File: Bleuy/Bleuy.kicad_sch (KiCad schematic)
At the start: 23 parts, among them J1 Conn_Coaxial, U1 STM32WB55CEU6, X1 32 MHz, X2 32.768 kHz

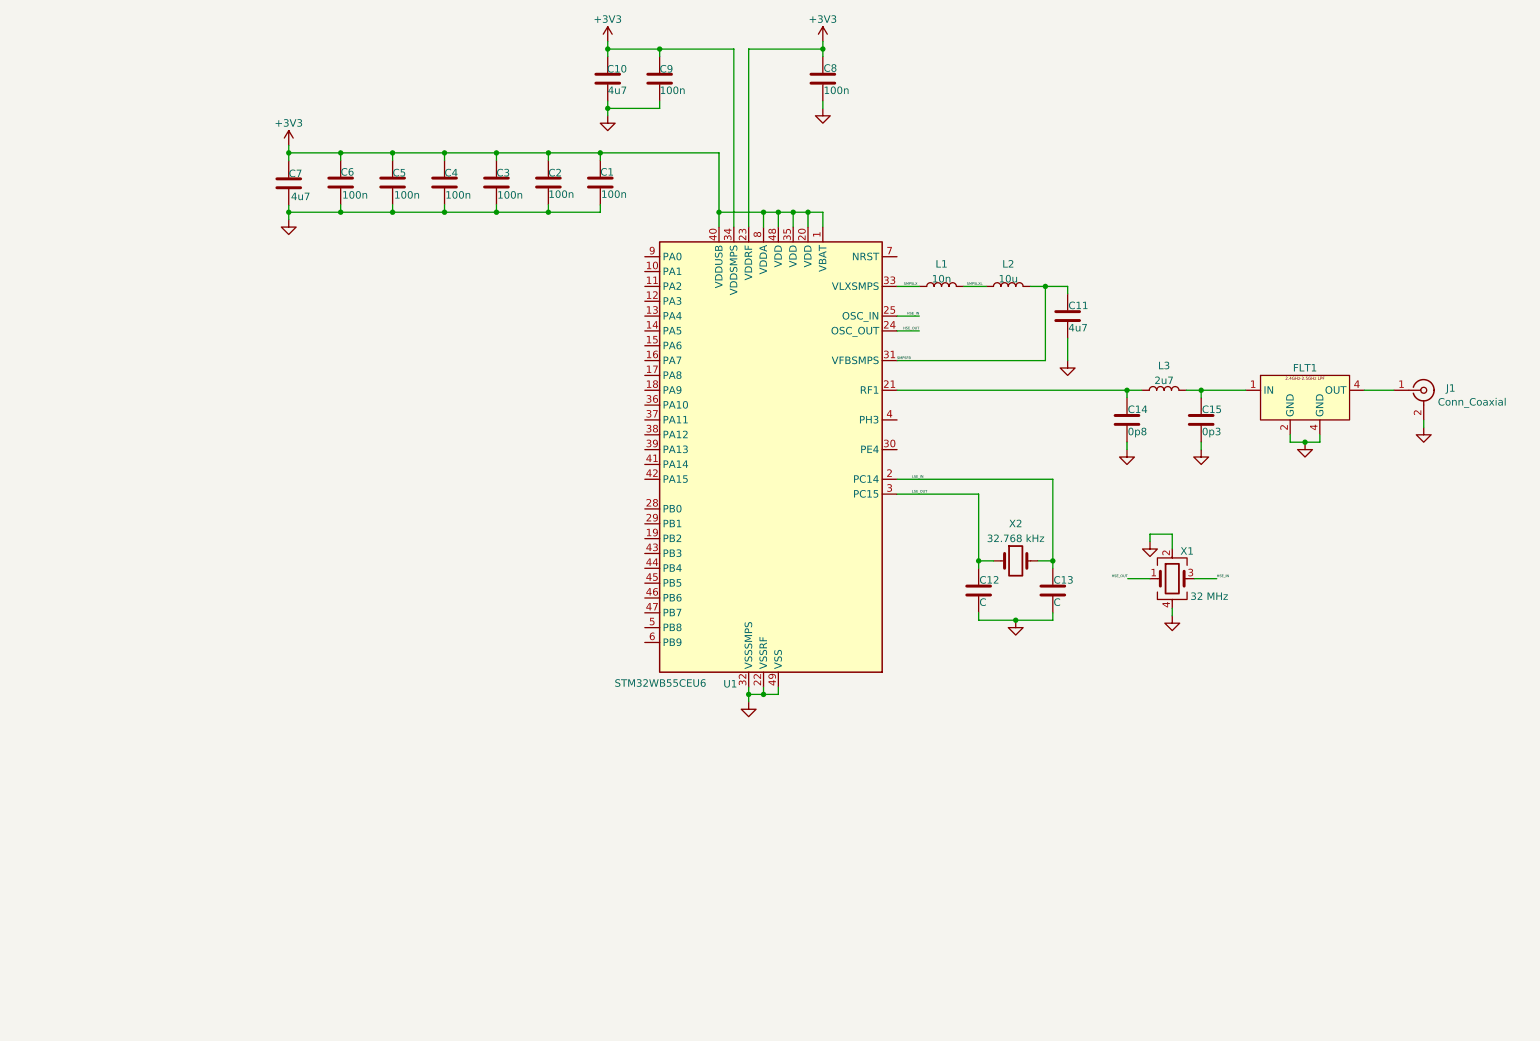
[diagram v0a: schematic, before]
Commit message: Bleuy Rev A
+ Added USB-C receptacle to power implemented 5V to 3.3V LDO
+ Added footprint for LPF
+ Added tag-connect SWD pins and UART breakout pins
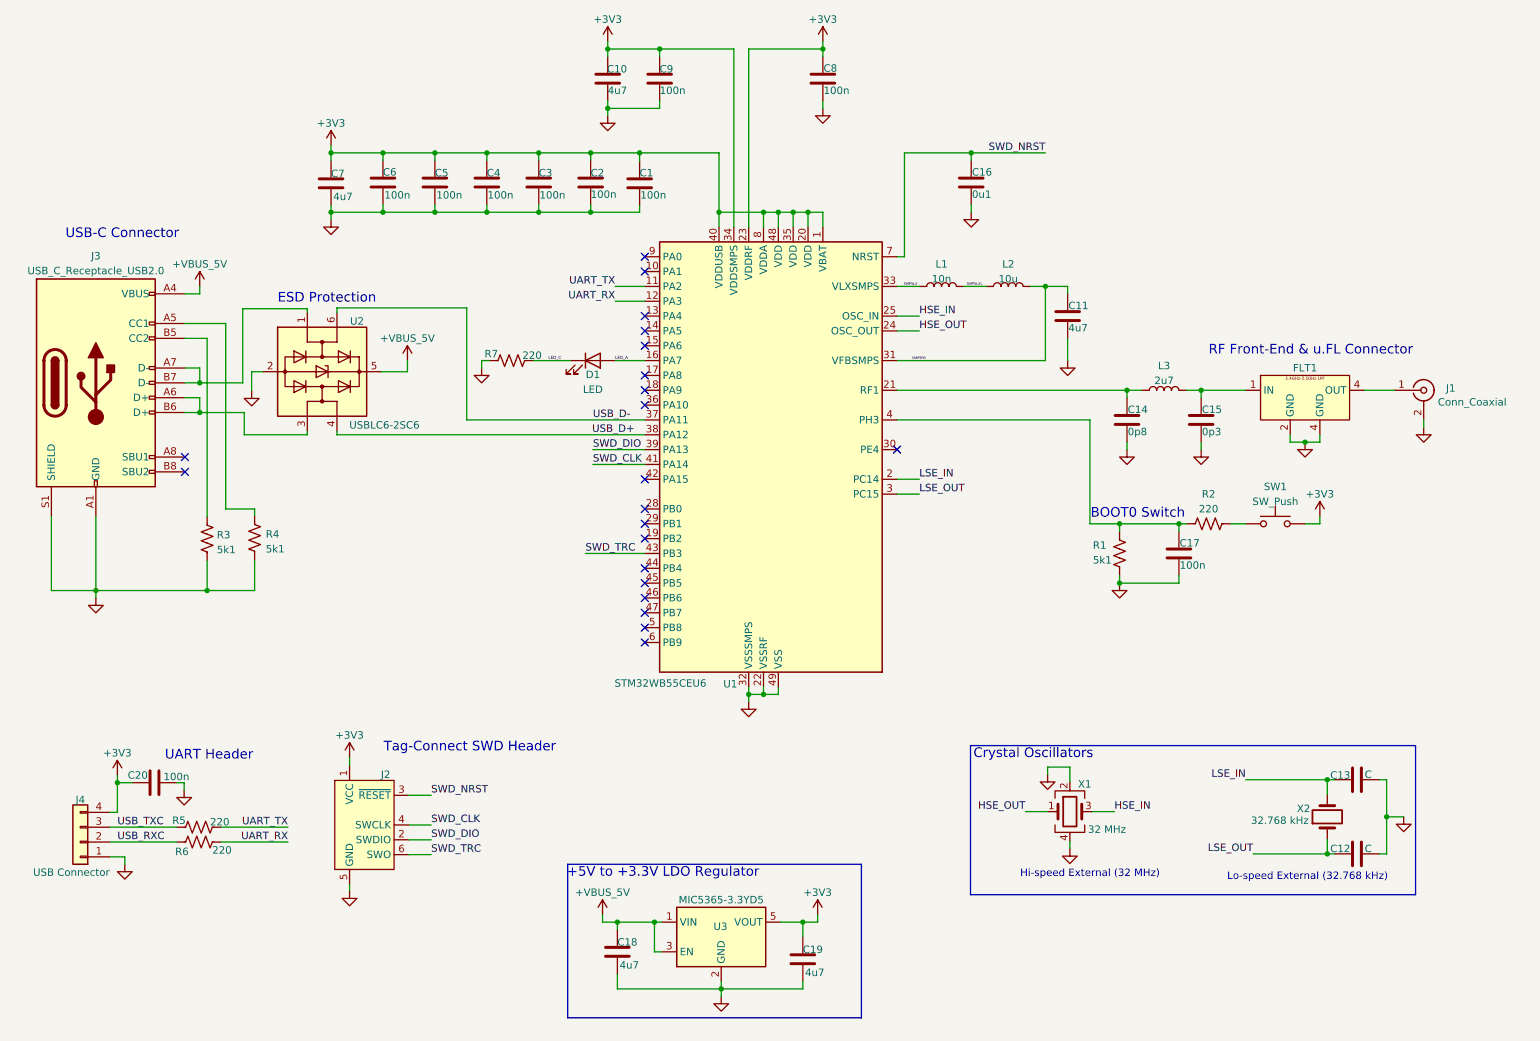
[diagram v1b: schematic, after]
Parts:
- added C16: 0u1, symbol Device:C
- added C17, C20: 100n, symbol Device:C
- added C18, C19: 4u7, symbol Device:C
- added D1: LED, symbol Device:LED
- added J2: Conn_ARM_SWD_TagConnect_TC2030, Connector:Tag-Connect_TC2030-IDC-FP_2x03_P1.27mm_Vertical, symbol Connector:Conn_ARM_SWD_TagConnect_TC2030
- added J3: USB_C_Receptacle_USB2.0, symbol Connector:USB_C_Receptacle_USB2.0
- added J4: USB Connector, symbol Connector_Generic:Conn_01x04
- added R1, R3, R4: 5k1, symbol Device:R_US
- added R2, R5, R6, R7: 220, symbol Device:R_US
- added SW1: SW_Push, symbol Switch:SW_Push
- added U2: USBLC6-2SC6, Package_TO_SOT_SMD:SOT-23-6, symbol Power_Protection:USBLC6-2SC6
- added U3: MIC5365-3.3YD5, Package_TO_SOT_SMD:SOT-23-5, symbol Regulator_Linear:MIC5365-3.3YD5
- FLT1: footprint (none) -> RF LPF:DLF162500LT-5028A1
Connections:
- net +3V3: now also C19.1, C20.1, J2.1 (VCC), J4.4 (Pin_4), SW1.2, U3.5 (VOUT)
- net GND: now also C16.2, C17.2, C18.2, C19.2, C20.2, J2.5 (GND), J3.A1 (GND), J3.A12 (GND), J3.B1 (GND), J3.B12 (GND), J3.S1 (SHIELD), J4.1 (Pin_1), R1.2, R3.2, R4.2, R7.1, U2.2 (GND), U3.2 (GND)
- net UART_TX: now reaches U1.11 (PA2)
- net UART_TX: now also R5.2
- net UART_RX: now reaches U1.12 (PA3)
- net UART_RX: now also R6.2
- net LED_A: now reaches U1.16 (PA7)
- net LED_A: now also D1.2 (A)
- net USB_D-: now reaches U1.37 (PA11)
- net USB_D-: now also U2.6 (I/O1)
- net USB_D+: now reaches U1.38 (PA12)
- net USB_D+: now also U2.4 (I/O2)
- net SWD_DIO: now reaches U1.39 (PA13)
- net SWD_DIO: now also J2.2 (SWDIO)
- net at U1.4 (PH3): now also C17.1, R1.1, R2.1
- net SWD_CLK: now reaches U1.41 (PA14)
- net SWD_CLK: now also J2.4 (SWCLK)
- net SWD_TRC: now reaches U1.43 (PB3)
- net SWD_TRC: now also J2.6 (SWO)
- net SWD_NRST: now reaches U1.7 (NRST)
- net SWD_NRST: now also C16.1, J2.3 (~{RESET})
- new net: J3.B5 (CC2), R3.1
- new net: J3.A5 (CC1), R4.1
- new net: J3.A7 (D-), J3.B7 (D-), U2.1 (I/O1)
- new net: J3.A6 (D+), J3.B6 (D+), U2.3 (I/O2)
- new net: R2.2, SW1.1
- new net +5V: C18.1, J3.A4 (VBUS), J3.A9 (VBUS), J3.B4 (VBUS), J3.B9 (VBUS), U2.5 (VBUS), U3.1 (VIN), U3.3 (EN)
- new net LED_C: D1.1 (K), R7.2
- new net USB_RXC: J4.2 (Pin_2), R6.1
- new net USB_TXC: J4.3 (Pin_3), R5.1
- no-connect marks 0 -> 21
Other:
- note added: "+5V to +3.3V LDO Regulator"
- note added: "BOOT0 Switch"
- note added: "Crystal Oscillators"
- note added: "ESD Protection"
- note added: "Hi-speed External (32 MHz)"
- note added: "Lo-speed External (32.768 kHz)"
- note added: "RF Front-End & u.FL Connector"
- note added: "Tag-Connect SWD Header"
- note added: "UART Header"
- note added: "USB-C Connector"
- title: (none) -> Bleuy
- moved on the sheet: C1, C12, C13, C2, C3, C4, C5, C6, C7, X1, X2

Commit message: Updated to Rev A Release
+ Finalized component placement
+ Added fiducial markers and mounting holes
+ Added ground stitching
+ Added power pours
+ Adjusted differential pair routing
+ Adjusted some routing to allow for better component placement
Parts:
- added FM1, FM2, FM3: Fiducial, Fiducial:Fiducial_1mm_Mask2mm, symbol Mechanical:Fiducial
- added H1, H2, H3, H4: MountingHole_Pad, MountingHole:MountingHole_2.2mm_M2_Pad_Via, symbol Mechanical:MountingHole_Pad
- C1, C16, C17, C2, C20, C3, C4, C5, C6, C8, C9: footprint (none) -> Capacitor_SMD:C_0402_1005Metric; Manufacturer (none) -> KYOCERA AVX; Manufacturer Part Number (none) -> 04023C104KAT2A
- C10, C11, C18, C19, C7: footprint (none) -> Capacitor_SMD:C_0603_1608Metric; Manufacturer (none) -> KYOCERA AVX; Manufacturer Part Number (none) -> 0603YD475MAT2A
- C12, C13: value C -> 10p; footprint (none) -> Capacitor_SMD:C_0402_1005Metric; Manufacturer (none) -> KYOCERA AVX; Manufacturer Part Number (none) -> 04025A100JAT4A
- C14: footprint (none) -> Capacitor_SMD:C_0402_1005Metric; Manufacturer (none) -> Murata; Manufacturer Part Number (none) -> GRM1555C1HR80BA01D
- C15: footprint (none) -> Capacitor_SMD:C_0402_1005Metric; Manufacturer (none) -> Murata; Manufacturer Part Number (none) -> GRM1555C1HR30WA01D
- D1: footprint (none) -> LED_SMD:LED_0402_1005Metric; Manufacturer (none) -> Wurth; Manufacturer Part Number (none) -> 150040RS73240
- FLT1: Manufacturer (none) -> TDK; Manufacturer Part Number (none) -> DLF162500LT-5028A1
- J1: footprint (none) -> Connector_Coaxial:U.FL_Hirose_U.FL-R-SMT-1_Vertical; Manufacturer (none) -> Hirose; Manufacturer Part Number (none) -> U.FL-R-SMT(01)
- J3: footprint (none) -> Connector_USB:USB_C_Receptacle_GCT_USB4105-xx-A_16P_TopMnt_Horizontal; Manufacturer (none) -> GCT; Manufacturer Part Number (none) -> USB4105-GF-A
- J4: footprint (none) -> Connector_Molex:Molex_PicoBlade_53261-0471_1x04-1MP_P1.25mm_Horizontal; Manufacturer (none) -> Molex; Manufacturer Part Number (none) -> 53048-0410
- L1: footprint (none) -> Inductor_SMD:L_0402_1005Metric; Manufacturer (none) -> Murata; Manufacturer Part Number (none) -> LQG15WZ10NJ02D
- L2: footprint (none) -> Inductor_SMD:L_0805_2012Metric; Manufacturer (none) -> Murata; Manufacturer Part Number (none) -> LQM21FN100M70L
- L3: value 2u7 -> 2n7; footprint (none) -> Inductor_SMD:L_0402_1005Metric; Manufacturer (none) -> Murata; Manufacturer Part Number (none) -> LQG15HS2N7S02
- R1, R3, R4: footprint (none) -> Resistor_SMD:R_0402_1005Metric; Manufacturer (none) -> YAGEO; Manufacturer Part Number (none) -> RC0603FR-075K1L
- R2, R5, R6, R7: footprint (none) -> Resistor_SMD:R_0402_1005Metric; Manufacturer (none) -> YAGEO; Manufacturer Part Number (none) -> RC0402FR-07221RL
- SW1: footprint (none) -> Button_Switch_SMD:SW_SPST_CK_RS282G05A3; Manufacturer (none) -> C&K; Manufacturer Part Number (none) -> RS282G05A3SMRT
- U1: Manufacturer (none) -> STMicroelectronics; Manufacturer Part Number (none) -> STM32WB55CEU6
- U2: Manufacturer (none) -> STMicroelectronics; Manufacturer Part Number (none) -> USBLC6-2SC6
- U3: Manufacturer (none) -> Microchip; Manufacturer Part Number (none) -> MIC5365-3.3YD5-TR
- X1: footprint (none) -> Crystal:Crystal_SMD_2016-4Pin_2.0x1.6mm; Manufacturer (none) -> NDK; Manufacturer Part Number (none) -> NX2016SA-32M-EZS00A-CS06465
- X2: footprint (none) -> Crystal:Crystal_SMD_2012-2Pin_2.0x1.2mm; Manufacturer (none) -> NDK; Manufacturer Part Number (none) -> NX2012SA-32.768K-STD-MUB-1
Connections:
- net GND: now also H1.1, H2.1, H3.1, H4.1
- net RF: now reaches C14.1, L3.1, U1.21 (RF1)
- net RF_MATCH: now reaches C15.1, FLT1.1 (IN), L3.2
- net RF_ANT: now reaches J1.1 (In)
- net RF_ANT: now also FLT1.3 (OUT); no longer FLT1.4 (OUT)
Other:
- note added: "Fiducial Markers"
- note added: "Mounting Holes (M2)"
